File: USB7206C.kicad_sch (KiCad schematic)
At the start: 32 parts, among them J1 USB_SPI_(Opt), SW1 RESET_HUB, U1 USB7206C/KDX, U2 MIC803-29D4VM3-TR, Y1 25MHz

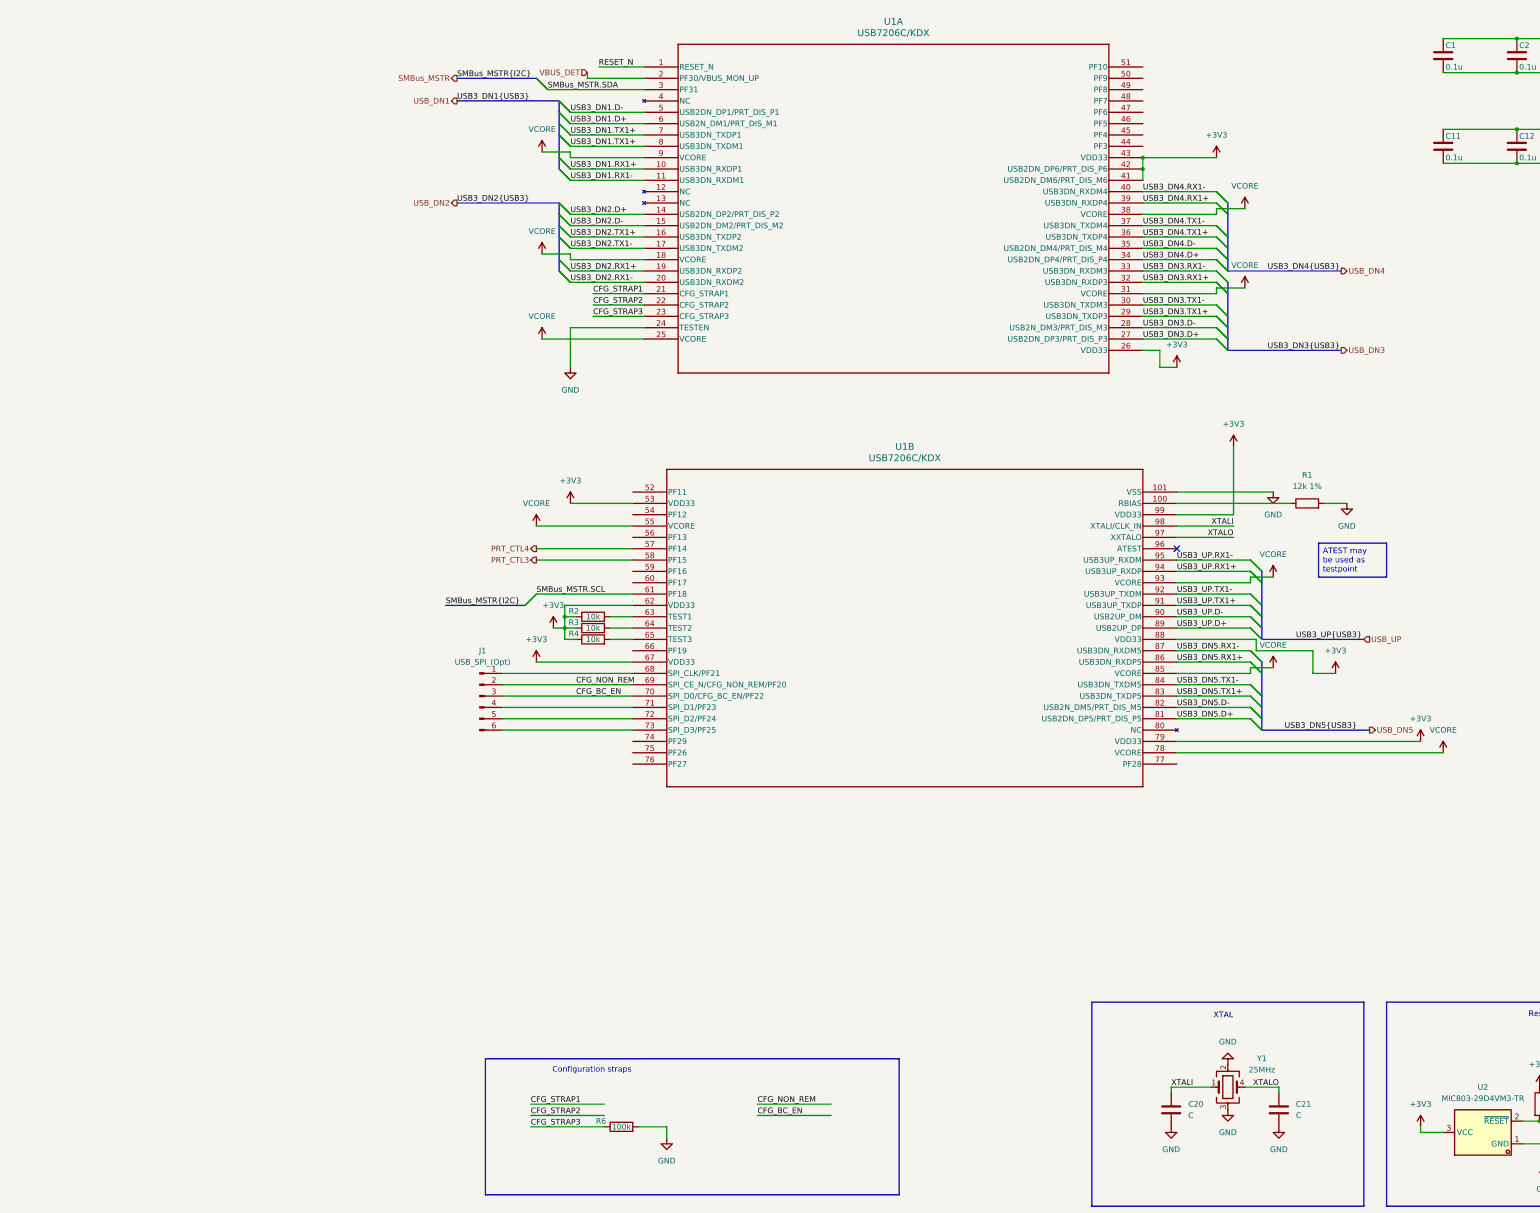
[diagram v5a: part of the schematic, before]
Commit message: Scheme fixes
Fixed wrong connection of SNS pin of U21
USB7206c symbol improved
R7's value fixed
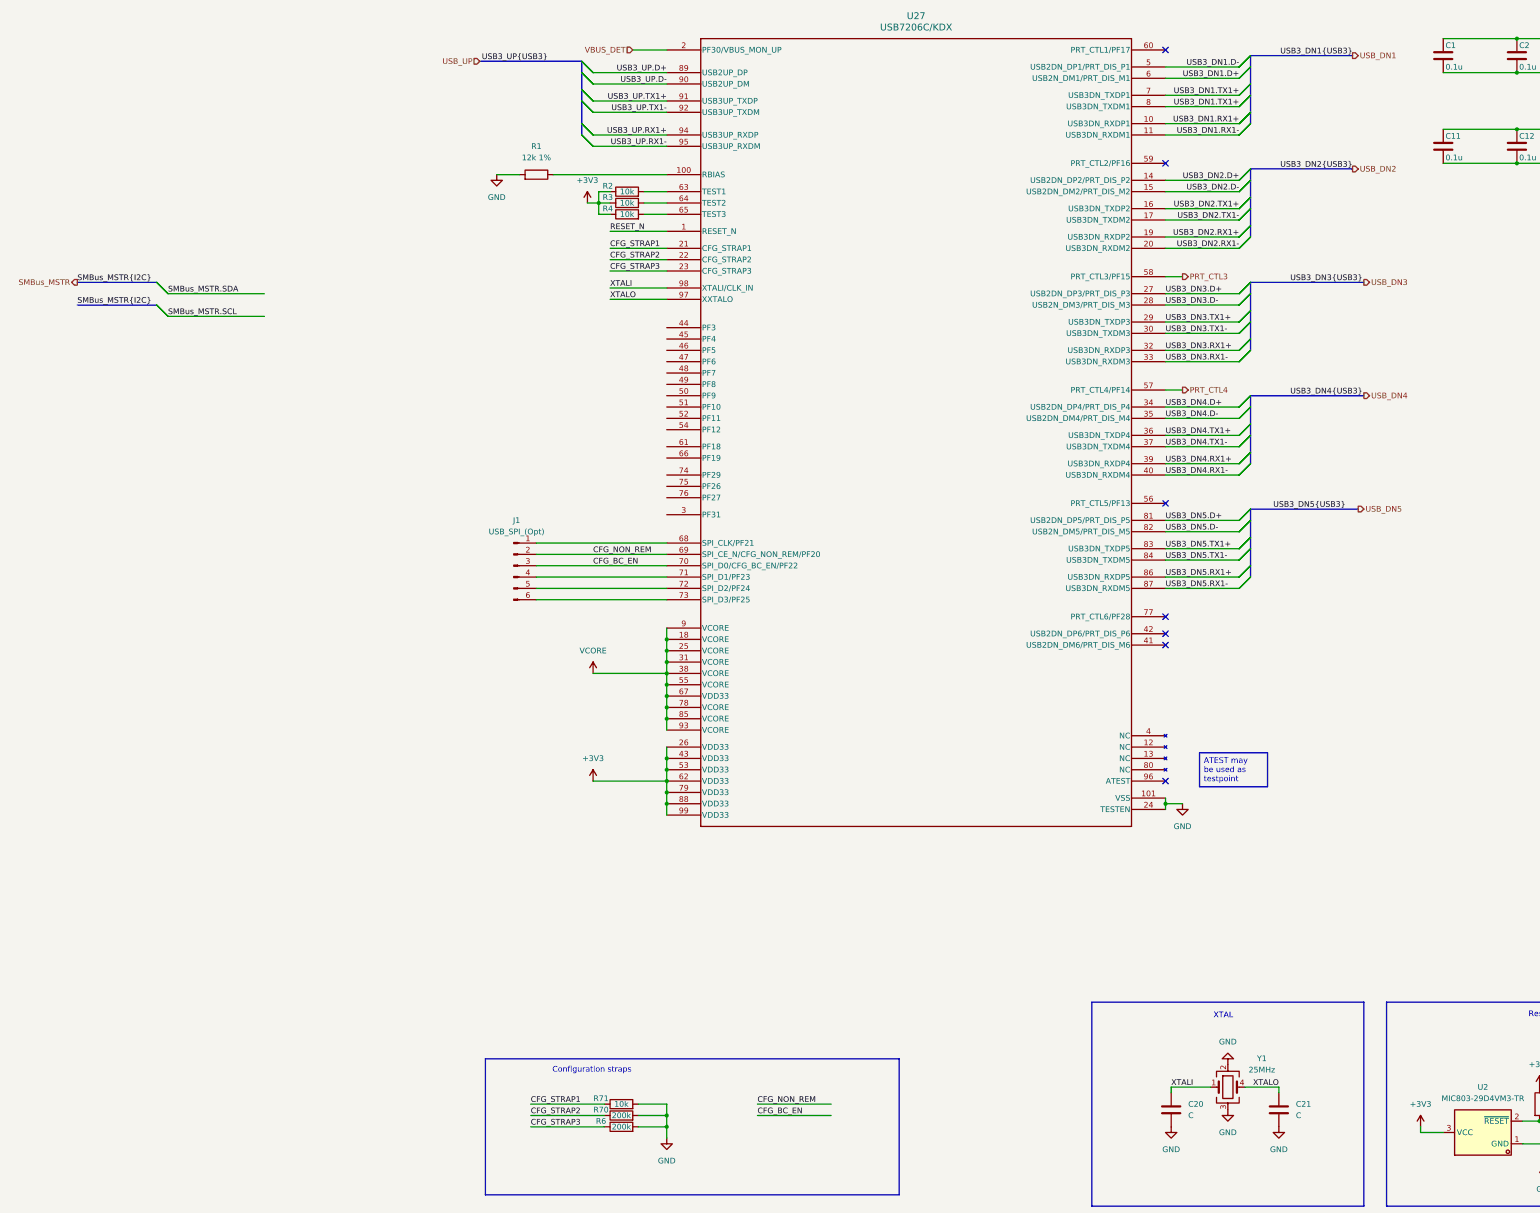
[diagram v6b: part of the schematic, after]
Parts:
- removed U1: USB7206C/KDX, Package_QFP:VQFP-100_14x14mm_P0.5mm, symbol 2025-07-15_10-11-24:USB7206C_KDX
- added R70: 200k, Resistor_SMD:R_0402_1005Metric, symbol Device:R
- added R71: 10k, Resistor_SMD:R_0402_1005Metric, symbol Device:R
- added U27: USB7206C/KDX, VQFN100_KDX_MCH, symbol 2025-07-15_10-11-24:USB7206C_KDX
- R6: value 100k -> 200k
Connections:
- net +3V3: now also U27.26 (VDD33), U27.43 (VDD33), U27.53 (VDD33), U27.62 (VDD33), U27.79 (VDD33), U27.88 (VDD33), U27.99 (VDD33)
- net CFG_BC_EN: now also U27.70 (SPI_D0/CFG_BC_EN/PF22)
- net CFG_NON_REM: now also U27.69 (SPI_CE_N/CFG_NON_REM/PF20)
- net CFG_STRAP1: now also R71.1, U27.21 (CFG_STRAP1)
- net CFG_STRAP2: now also R70.1, U27.22 (CFG_STRAP2)
- net CFG_STRAP3: now also U27.23 (CFG_STRAP3)
- net GND: now also R70.2, R71.2, U27.101 (VSS), U27.24 (TESTEN)
- net PRT_CTL3: now also U27.58 (PRT_CTL3/PF15)
- net PRT_CTL4: now also U27.57 (PRT_CTL4/PF14)
- net RESET_N: now also U27.1 (RESET_N)
- net USB3_DN1.D+: now also U27.6 (USB2N_DM1/PRT_DIS_M1)
- net USB3_DN1.D-: now also U27.5 (USB2DN_DP1/PRT_DIS_P1)
- net USB3_DN1.RX1+: now also U27.10 (USB3DN_RXDP1)
- net USB3_DN1.RX1-: now also U27.11 (USB3DN_RXDM1)
- net USB3_DN1.TX1+: now also U27.7 (USB3DN_TXDP1), U27.8 (USB3DN_TXDM1)
- net USB3_DN2.D+: now also U27.14 (USB2DN_DP2/PRT_DIS_P2)
- net USB3_DN2.D-: now also U27.15 (USB2DN_DM2/PRT_DIS_M2)
- net USB3_DN2.RX1+: now also U27.19 (USB3DN_RXDP2)
- net USB3_DN2.RX1-: now also U27.20 (USB3DN_RXDM2)
- net USB3_DN2.TX1+: now also U27.16 (USB3DN_TXDP2)
- net USB3_DN2.TX1-: now also U27.17 (USB3DN_TXDM2)
- net USB3_DN3.D+: now also U27.27 (USB2DN_DP3/PRT_DIS_P3)
- net USB3_DN3.D-: now also U27.28 (USB2N_DM3/PRT_DIS_M3)
- net USB3_DN3.RX1+: now also U27.32 (USB3DN_RXDP3)
- net USB3_DN3.RX1-: now also U27.33 (USB3DN_RXDM3)
- net USB3_DN3.TX1+: now also U27.29 (USB3DN_TXDP3)
- net USB3_DN3.TX1-: now also U27.30 (USB3DN_TXDM3)
- net USB3_DN4.D+: now also U27.34 (USB2DN_DP4/PRT_DIS_P4)
- net USB3_DN4.D-: now also U27.35 (USB2DN_DM4/PRT_DIS_M4)
- net USB3_DN4.RX1+: now also U27.39 (USB3DN_RXDP4)
- net USB3_DN4.RX1-: now also U27.40 (USB3DN_RXDM4)
- net USB3_DN4.TX1+: now also U27.36 (USB3DN_TXDP4)
- net USB3_DN4.TX1-: now also U27.37 (USB3DN_TXDM4)
- net USB3_DN5.D+: now also U27.81 (USB2DN_DP5/PRT_DIS_P5)
- net USB3_DN5.D-: now also U27.82 (USB2N_DM5/PRT_DIS_M5)
- net USB3_DN5.RX1+: now also U27.86 (USB3DN_RXDP5)
- net USB3_DN5.RX1-: now also U27.87 (USB3DN_RXDM5)
- net USB3_DN5.TX1+: now also U27.83 (USB3DN_TXDP5)
- net USB3_DN5.TX1-: now also U27.84 (USB3DN_TXDM5)
- net USB3_UP.D+: now also U27.89 (USB2UP_DP)
- net USB3_UP.D-: now also U27.90 (USB2UP_DM)
- net USB3_UP.RX1+: now also U27.94 (USB3UP_RXDP)
- net USB3_UP.RX1-: now also U27.95 (USB3UP_RXDM)
- net USB3_UP.TX1+: now also U27.91 (USB3UP_TXDP)
- net USB3_UP.TX1-: now also U27.92 (USB3UP_TXDM)
- net VBUS_DET: now also U27.2 (PF30/VBUS_MON_UP)
- net VCORE: now also U27.18 (VCORE), U27.25 (VCORE), U27.31 (VCORE), U27.38 (VCORE), U27.55 (VCORE), U27.67 (VDD33), U27.78 (VCORE), U27.85 (VCORE), U27.9 (VCORE), U27.93 (VCORE)
- net XTALI: now also U27.98 (XTALI/CLK_IN)
- net XTALO: now also U27.97 (XXTALO)
- net at R4.2: now also U27.65 (TEST3)
- net at J1.1 (Pin_1): now also U27.68 (SPI_CLK/PF21)
- net at J1.4 (Pin_4): now also U27.71 (SPI_D1/PF23)
- net at J1.5 (Pin_5): now also U27.72 (SPI_D2/PF24)
- net at J1.6 (Pin_6): now also U27.73 (SPI_D3/PF25)
- net at R1.1: now also U27.100 (RBIAS)
- net at R2.2: now also U27.63 (TEST1)
- net at R3.2: now also U27.64 (TEST2)
- no-connect marks 1 -> 7
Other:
- moved on the sheet: J1, R1, R2, R3, R4

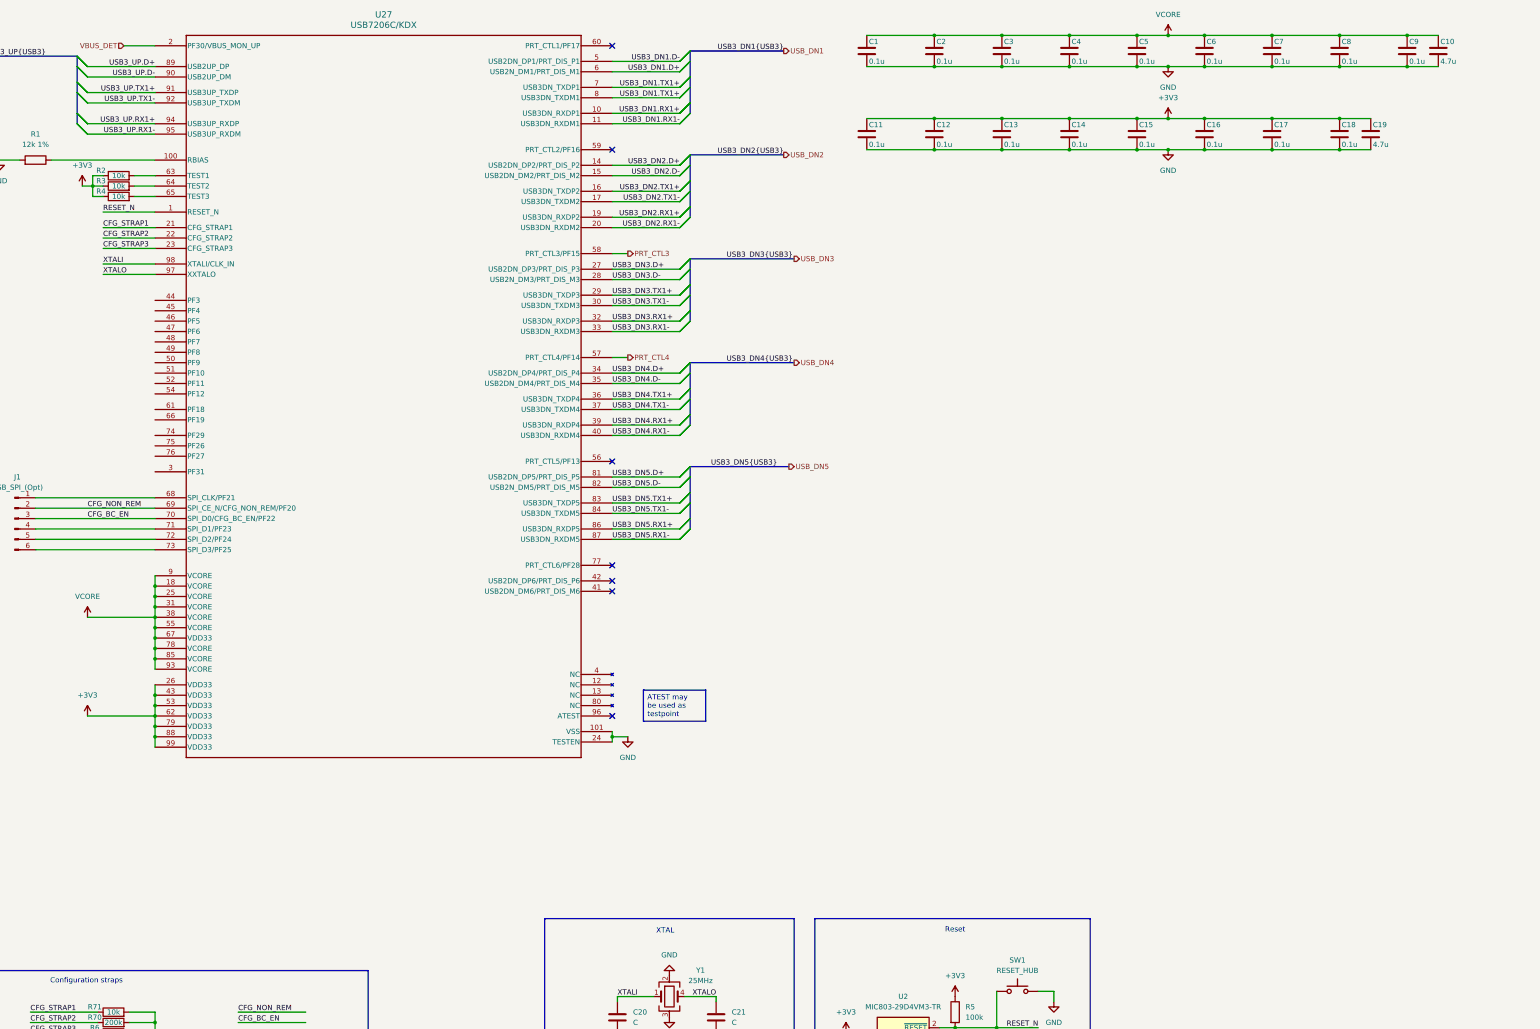
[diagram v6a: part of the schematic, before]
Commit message: MCP19035 changed to MP8795
TPS7A4701xRGW to AP7361C-33E
Led Indicator added
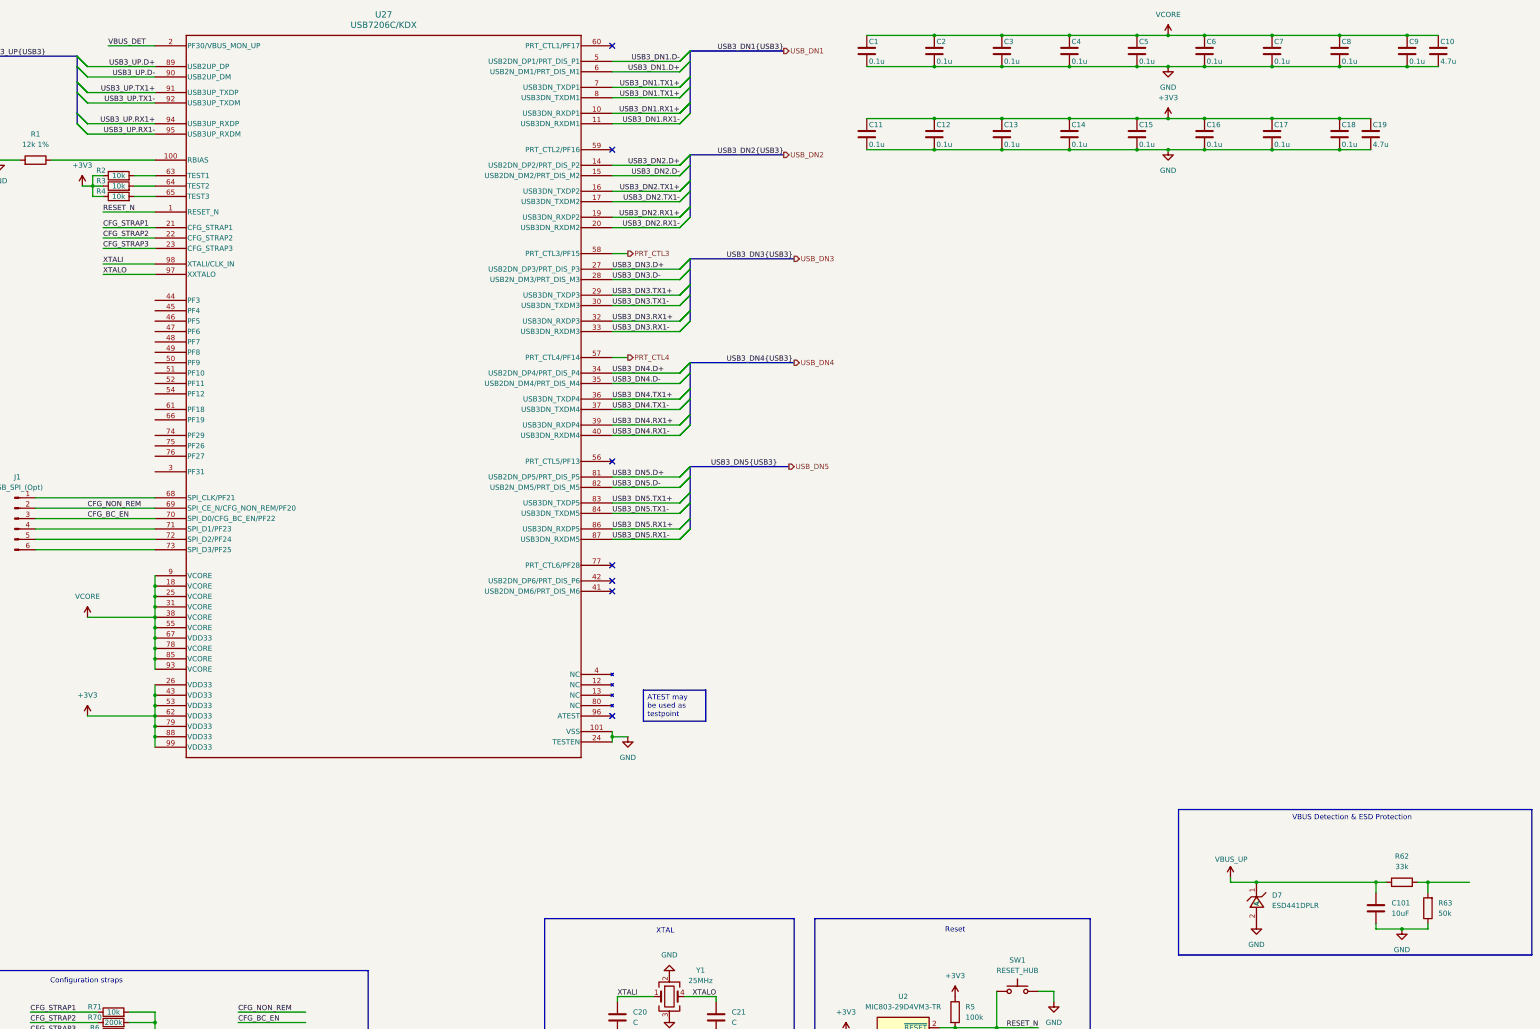
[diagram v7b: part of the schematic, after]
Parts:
- added C101: 10uF, Capacitor_SMD:C_0402_1005Metric, symbol Device:C
- added D7: ESD441DPLR, EasyEDA:X2SON-2_L0.6-W0.3-P0.35, symbol EasyEDA:ESD441DPLR
- added R62: 33k, Resistor_SMD:R_0402_1005Metric, symbol Device:R
- added R63: 50k, Resistor_SMD:R_0402_1005Metric, symbol Device:R
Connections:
- net GND: now also C101.2, D7.2 (A), R63.1
- new net: R62.2, R63.2
- new net VBUS_UP: C101.1, D7.1 (C), R62.1
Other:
- note added: "VBUS Detection & ESD Protection"

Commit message: I2C Addresses added to scheme
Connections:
- net VBUS_DET: now also R62.2, R63.2
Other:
- note added: "0x2D"
- note added: "SPI Address 0x3FFFA for DFU 0x0000 for the external SPI ROM"
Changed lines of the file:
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@@
+		)
+	)
+	(text "SPI Address\n0x3FFFA for DFU\n0x0000 for the external SPI ROM"
+		(exclude_from_sim no)
+		(at 7.874 138.684 0)
+		(effects
+			(font
+				(size 1.27 1.27)
+			)
+		)
+	)
+	(text "0x2D"
+		(exclude_from_sim no)
+		(at -93.726 77.978 0)
+		(effects
+			(font
+				(size 1.27 1.27)
+			)
 		)
 	)
@@
 	(wire
 		(pts
-			(xy 372.11 227.33) (xy 382.27 227.33)
+			(xy 372.11 227.33) (xy 391.16 227.33)
 		)
 		(stroke
@@
 		(effects
 			(font
+				(size 1.27 1.27)
+			)
+			(justify right bottom)
+		)
+	)
+	(label "VBUS_DET"
+		(at 391.16 227.33 180)
+		(effects
+			(font
